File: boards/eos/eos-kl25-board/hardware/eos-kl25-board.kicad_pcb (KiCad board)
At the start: 2 copper layers, 68.6 x 53.3 mm, 82 parts, among them J1 USB-C, J2 USB-C, J3 D8-SCL, J4 D0-D7, J5 POWER, J6 A0-A5, J7 SWD, J8 EXT, Q1 AO3400A, Q2 AO3400A, Q3 AO3400A, SW1 RESET, U1 SP0503BAHTG, U2 SP0503BAHTG, U3 TPS2116, U4 AP7361C-33, U5 MKL25Z128VLK4, U6 CP2102N-A02-GQFN20, U7 LIS2HH12, Y1 8MHz

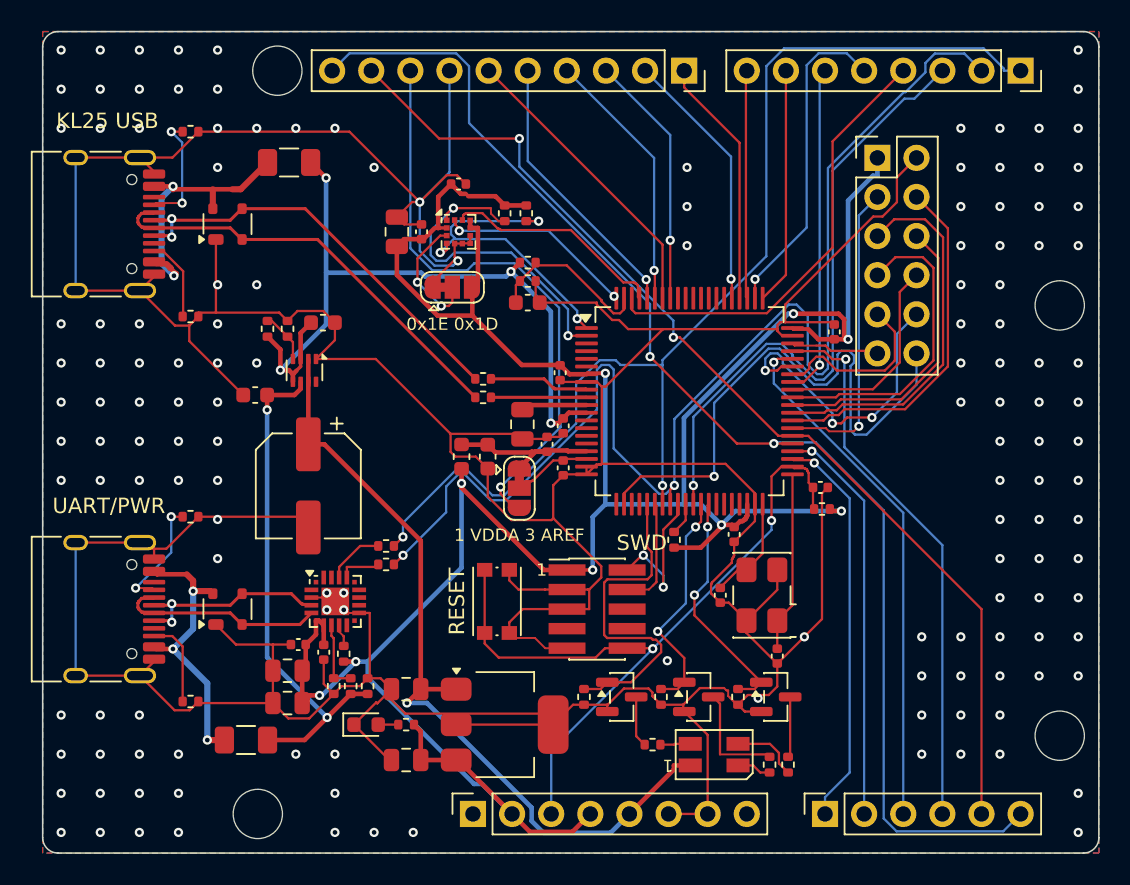
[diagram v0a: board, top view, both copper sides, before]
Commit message: fix(boards): rebuild the ten boards made before the no-via-in-pad rule (#55)
PR #64's generator keeps vias out of surface pads (a chip's exposed pad
aside) and 0.1 mm from their own net's pads. Ten boards on master were built
before that rule and had 34 pads with a via in or beside them. They are
rebuilt with the same generator: ATmega328P, RA2E1, KE16Z, KL25, STM32 64,
ESP32 DevKit, Learn RP2350, LPC55S69, CM4 Base and CM5 Base. Each builds at
ERC 0, DRC errors 0, unconnected 0 and parity 0, with the same parts, values,
nets and positions and the same DRC warnings as before.

Where the router could no longer close a short link without a via in a pad,
or left a ground pad without a good path to a via, the design files use
routing options only: priority routes, fanout_first, ground_vias, and a
bottom-layer router keep-out under KL25's crystal (so RESET_b no longer runs
under it). ViaInPadTest drops BUILT_BEFORE_THE_RULE; it now allows only Learn
RP2350's two Raspberry Pi reference vias, named by position. READMEs, TASKS
and CHANGELOG follow the rebuilt copper. Independent verification: three
rounds; the owner adopted a two-layer pour-island criterion (TASKS.md).

Part of #55.
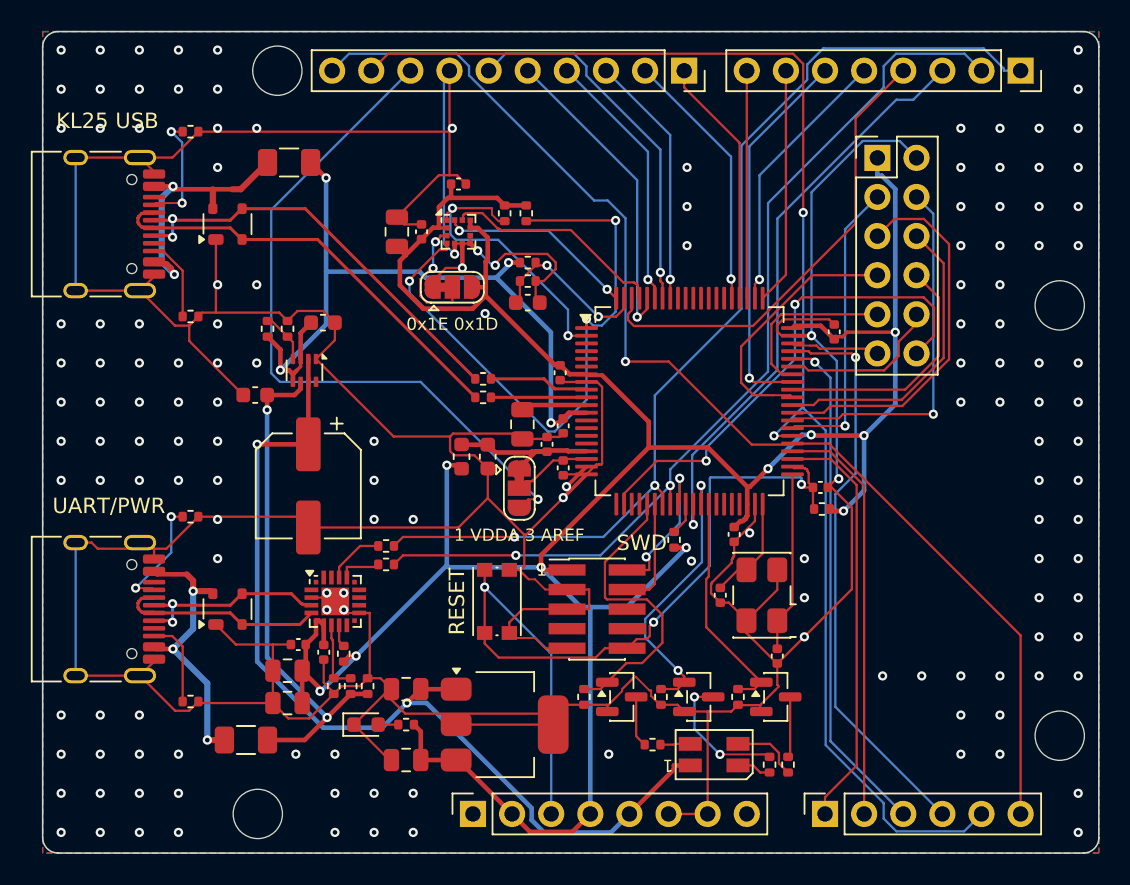
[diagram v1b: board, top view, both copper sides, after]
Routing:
- net /D1: track 83.6 -> 61.4 mm
- net /A4_SDA: track 69.1 -> 91.0 mm
- net /ACC_SDA: track 21.0 -> 40.6 mm
- net +5V: track 53.0 -> 63.0 mm, vias 1 -> 2
- net /EXT_PTC0: track 20.2 -> 10.6 mm, vias 3 -> 0
- net /D0: track 74.9 -> 66.4 mm
- net /AREF: track 38.5 -> 45.6 mm
- net GND: track 380.8 -> 387.5 mm, vias 144 -> 149
- net /RESET: track 49.6 -> 55.9 mm, vias 2 -> 3
- net +3V3: track 180.9 -> 186.7 mm, vias 9 -> 10
- net /A5_SCL: track 83.7 -> 78.3 mm, vias 2 -> 1
- net /EXT_PTE30: track 37.8 -> 32.4 mm, vias 1 -> 2
- net /D13: track 19.5 -> 24.3 mm, vias 0 -> 1
- net /EXT_PTB16: track 20.6 -> 16.9 mm
- net /D5: track 21.5 -> 24.9 mm
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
